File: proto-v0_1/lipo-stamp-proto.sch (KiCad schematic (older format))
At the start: 27 parts, among them Q1 Q_PMOS_GSD, U3 MCP73832-2-OT, U4 AP2112K-3.3, U5 AP9101CK6, U6 FS8205

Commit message: Going to start routing
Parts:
- added D1, D10, D11, D12, D13, D4, D5, D6, D7, D8, D9: LED, LED_SMD:LED_0805_2012Metric, symbol Device:LED
- added JP1, JP2, JP3, JP4: SolderJumper_2_Open, Jumper:SolderJumper-2_P1.3mm_Open_TrianglePad1.0x1.5mm, symbol Jumper:SolderJumper_2_Open
- added JP10, JP11, JP12, JP13, JP14, JP15, JP16, JP5, JP6, JP7, JP8, JP9: Jumper_NC_Small, Jumper:SolderJumper-2_P1.3mm_Bridged_RoundedPad1.0x1.5mm, symbol Device:Jumper_NC_Small
- added R10, R11, R12, R13, R15, R16, R17, R18, R19, R20, R9: R, Resistor_SMD:R_0805_2012Metric, symbol Device:R
- added R14, R6: 10K, Resistor_SMD:R_0805_2012Metric, symbol Device:R
- added R7: 2K2, Resistor_SMD:R_0805_2012Metric, symbol Device:R
- added R8: 1K, Resistor_SMD:R_0805_2012Metric, symbol Device:R
- added TP1, TP11, TP12, TP13, TP2, TP20, TP21, TP22, TP23, TP24, TP25, TP26, TP27, TP28, TP29, TP3, TP30, TP31, TP32, TP33, TP34, TP35, TP36, TP37, TP38, TP4, TP5, TP6: TestPoint, Everything:castellated-2-pin, symbol Connector:TestPoint
- added Z1, Z10, Z11, Z12, Z13, Z14, Z19, Z3, Z4, Z6, Z7, Z9: 0, Resistor_SMD:R_0805_2012Metric, symbol Device:R_Small
- R1: value R -> 4K7
- R3: value 330Ohm -> 330
- TP10, TP14, TP15, TP16, TP17, TP18, TP19, TP7, TP8, TP9: footprint Connector_PinHeader_2.54mm:PinHeader_1x01_P2.54mm_Vertical -> Everything:castellated-2-pin
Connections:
- net +BATT: now also TP16.1, D8.2 (A), TP12.1, TP2.1, TP6.1, Z13.1, Z4.1, Z9.1; no longer C2.1, Q1.3 (D), R3.1, TP15.1, TP8.1, U3.3 (VBAT)
- net +CHARGE: now also TP14.1, D13.2 (A), TP4.1, Z1.2, Z3.2; no longer C1.1, D2.2 (A), D3.2 (A), Q1.1 (G), R5.2, TP10.1, U3.4 (VDD)
- net -BATT: now also JP11.1, TP1.1, TP11.1, Z14.1; no longer C5.2, TP7.1, U5.6 (VSS), U6.1 (S1)
- net 3V3_OUT: now also TP17.1, TP7.1, D11.2 (A), Z12.1; no longer C4.1, TP16.1, U4.5 (VOUT)
- net 3V3_REG_EN: now also TP18.1, TP8.1, D10.2 (A), Z11.2; no longer TP17.1, U4.3 (EN)
- net GND: now also TP10.1, JP10.1, JP13.1, JP14.1, JP15.1, JP16.1, JP5.1, JP7.1, JP8.1, JP9.1, R6.2, R7.2, R8.2, TP13.1, TP20.1, TP3.1, TP30.1, Z19.1; no longer R4.2, TP19.1, TP9.1, U6.3 (S2)
- net STAT_OUT: now also TP19.1, TP9.1, JP12.1, Z6.2; no longer R2.2, TP18.1, U3.1 (STAT)
- net VMAX_OUT: now also TP15.1, D12.2 (A), D9.2 (A), TP5.1, Z10.2, Z7.1; no longer C3.1, D2.1 (K), Q1.2 (S), TP14.1, U4.1 (VIN)
- net at C5.1, R3.2, U5.5 (VDD): now also TP23.1
- net at R4.1, U5.2 (VM): now also TP22.1
- net at U3.5 (PROG): now also JP1.1 (A), JP2.1 (A), JP3.1 (A), JP4.1 (A), TP29.1; no longer R1.1
- net at U5.1 (DO), U6.6 (G1): now also TP25.1
- net at U5.3 (CO), U6.4 (G2): now also TP24.1
- new net: D2.1 (K), Q1.2 (S), TP28.1, Z7.2
- new net: D2.2 (A), Q1.1 (G), R5.2, TP26.1, Z1.1
- new net: Q1.3 (D), TP27.1, Z4.2
- new net: C3.1, D5.2 (A), R14.2, TP36.1, U4.1 (VIN), Z10.1
- new net: C4.1, D6.2 (A), TP38.1, U4.5 (VOUT), Z12.2
- new net: C5.2, TP21.1, U5.6 (VSS), U6.1 (S1), Z14.2
- new net: R4.2, TP34.1, U6.3 (S2), Z19.2
- new net: R3.1, TP35.1, Z13.2
- new net: C2.1, D4.2 (A), TP32.1, U3.3 (VBAT), Z9.2
- new net: C1.1, D1.2 (A), D3.2 (A), TP31.1, U3.4 (VDD), Z3.1
- new net: JP6.2, R2.2
- new net: JP6.1, TP33.1, U3.1 (STAT), Z6.1
- new net: JP2.2 (B), R1.1
- new net: D7.2 (A), R14.1, TP37.1, U4.3 (EN), Z11.1
- new net: JP1.2 (B), R6.1
- new net: JP4.2 (B), R8.1
- new net: JP3.2 (B), R7.1
- new net: D1.1 (K), R9.1
- new net: JP5.2, R9.2
- new net: D4.1 (K), R10.1
- new net: JP7.2, R10.2
- new net: D5.1 (K), R11.1
- new net: JP8.2, R11.2
- new net: D6.1 (K), R12.1
- new net: JP9.2, R12.2
- new net: D7.1 (K), R13.1
- new net: JP10.2, R13.2
- new net: D9.1 (K), R16.1
- new net: JP12.2, R16.2
- new net: D10.1 (K), R17.1
- new net: JP13.2, R17.2
- new net: D11.1 (K), R18.1
- new net: JP14.2, R18.2
- new net: D12.1 (K), R19.1
- new net: JP15.2, R19.2
- new net: D13.1 (K), R20.1
- new net: JP16.2, R20.2
- new net: D8.1 (K), R15.1
- new net: JP11.2, R15.2
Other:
- note added: "1000mA"
- note added: "100mA"
- note added: "213mA"
- note added: "455mA"
- note removed: "TODO: Resistor Values"
- note removed: "TODO: Should -CHARGE be common with GND?"
- note removed: "TODO: Should VBAT be common with +BATT?\nDownstream of battery protection?"
- moved on the sheet: C1, C2, C3, C4, C5, D2, D3, Q1, R1, R2, R3, R4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

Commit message: Almost done, just needs back silkscreen
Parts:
- removed JP11: Jumper_NC_Small, Jumper:SolderJumper-2_P1.3mm_Bridged_RoundedPad1.0x1.5mm, symbol Device:Jumper_NC_Small
- added JP11: Jumper_NO_Small, Jumper:SolderJumper-2_P1.3mm_Open_RoundedPad1.0x1.5mm, symbol Device:Jumper_NO_Small
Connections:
- net -BATT: now also JP11.2
- net at R15.2: now also JP11.1
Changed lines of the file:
@@
 	1    0    0    -1
-$EndComp
-$Comp
-L Device:Jumper_NC_Small JP11
-U 1 1 604FB90A
-P 5000 3500
-F 0 "JP11" V 5046 3453 50  0000 R CNN
-F 1 "Jumper_NC_Small" V 4955 3453 50  0000 R CNN
-F 2 "Jumper:SolderJumper-2_P1.3mm_Bridged_RoundedPad1.0x1.5mm" H 5000 3500 50  0001 C CNN
-F 3 "~" H 5000 3500 50  0001 C CNN
-	1    5000 3500
-	0    -1   -1   0
 $EndComp
 Text Label 5000 2800 1    50   ~ 0
@@
 Text Label 5000 3600 3    50   ~ 0
 -BATT
+$Comp
+L Device:Jumper_NO_Small JP11
+U 1 1 6068AF95
+P 5000 3500
+F 0 "JP11" V 4954 3548 50  0000 L CNN
+F 1 "Jumper_NO_Small" V 5045 3548 50  0000 L CNN
+F 2 "Jumper:SolderJumper-2_P1.3mm_Open_RoundedPad1.0x1.5mm" H 5000 3500 50  0001 C CNN
+F 3 "~" H 5000 3500 50  0001 C CNN
+	1    5000 3500
+	0    1    1    0
+$EndComp
 $EndSCHEMATC

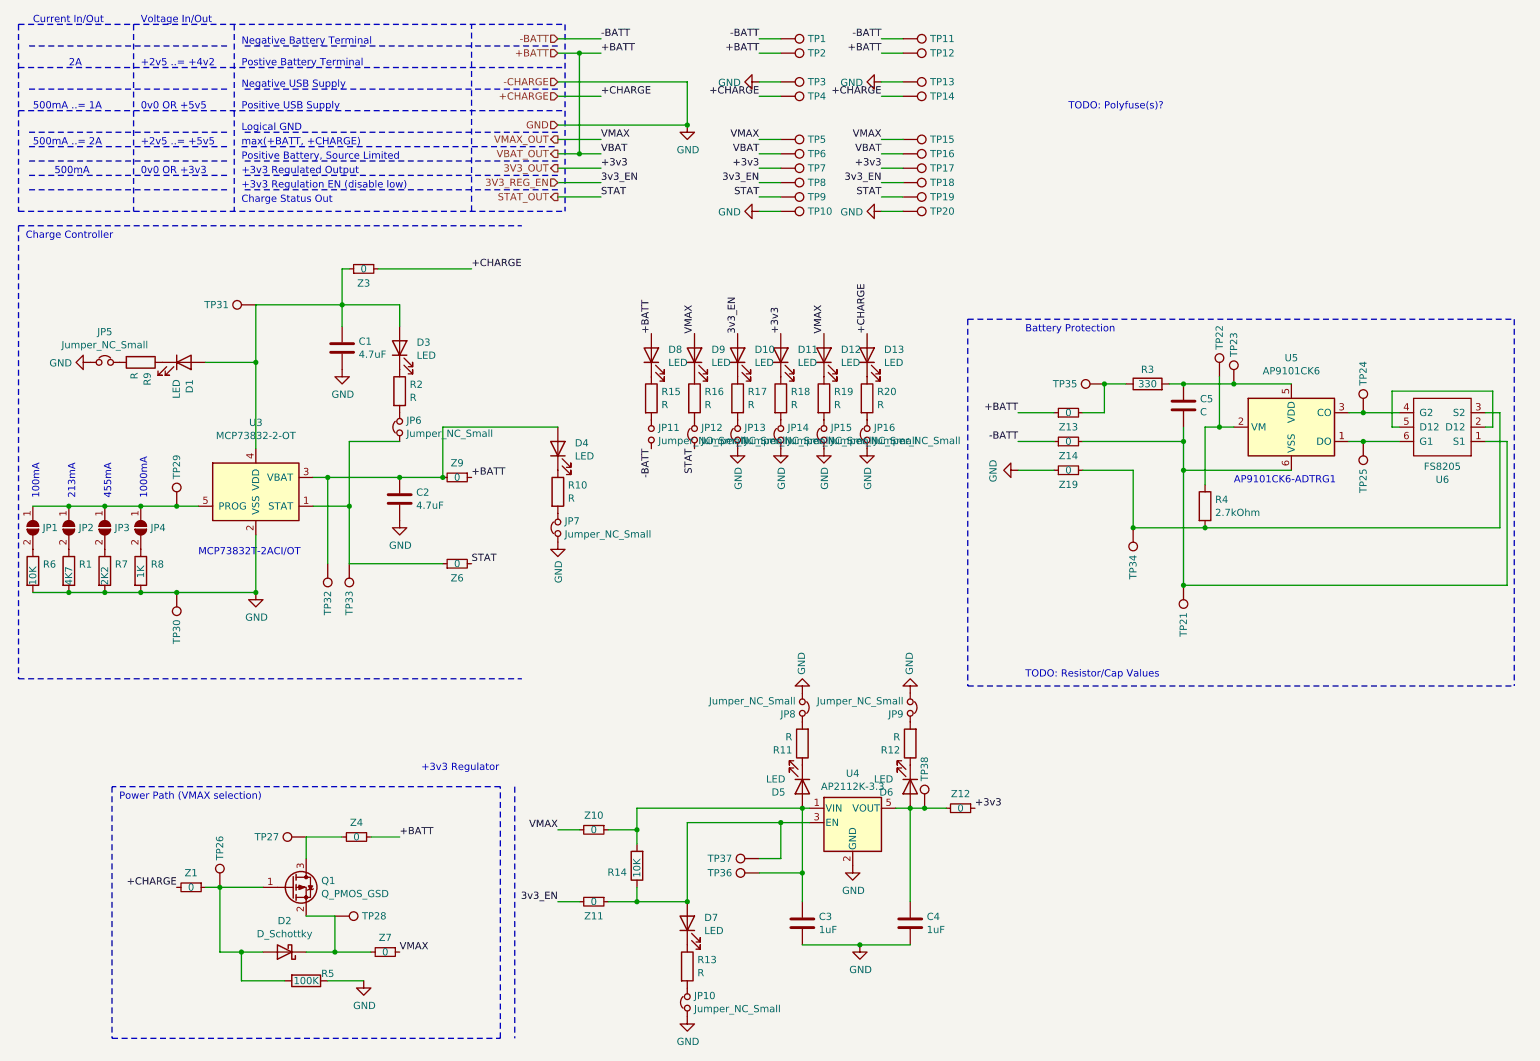
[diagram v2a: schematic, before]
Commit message: Add 2A polyfuse
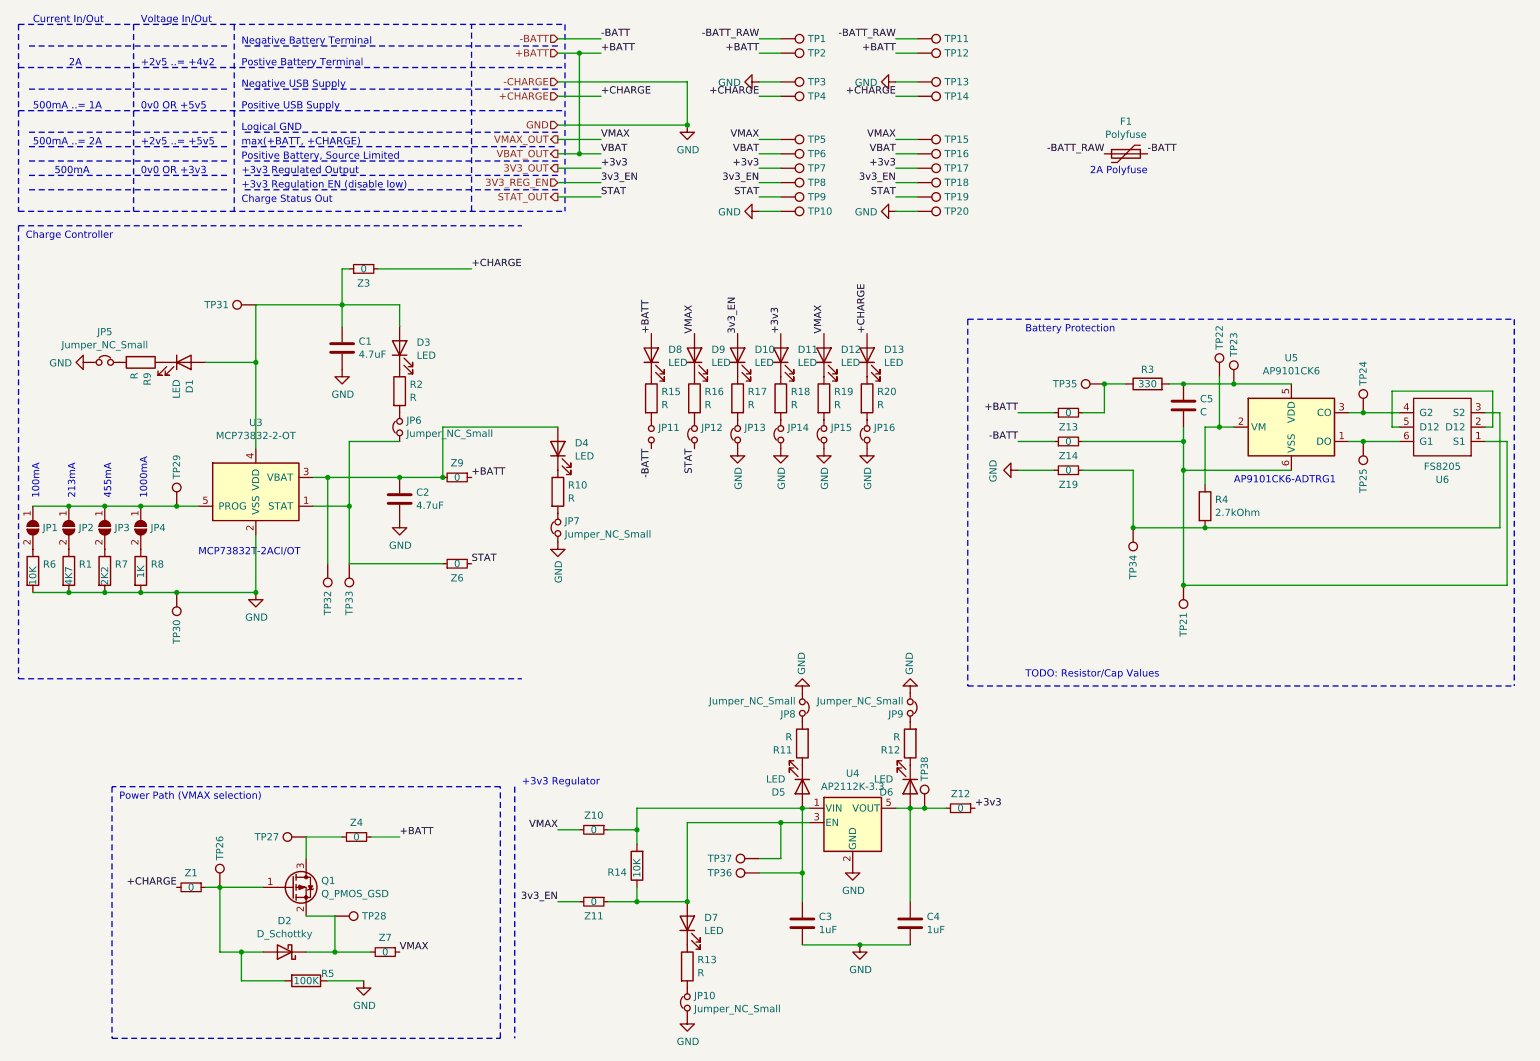
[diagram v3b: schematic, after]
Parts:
- added F1: Polyfuse, Fuse:Fuse_1206_3216Metric_Castellated, symbol Device:Polyfuse
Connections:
- net -BATT: now also F1.1; no longer TP1.1, TP11.1
- new net -BATT_RAW: F1.2, TP1.1, TP11.1
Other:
- note added: "2A Polyfuse"
- note removed: "TODO: Polyfuse(s)?"
- moved on the sheet: TP11, TP12, TP13, TP14, TP15, TP16, TP17, TP18, TP19, TP20

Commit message: Rerouted TP4056, considering redoing
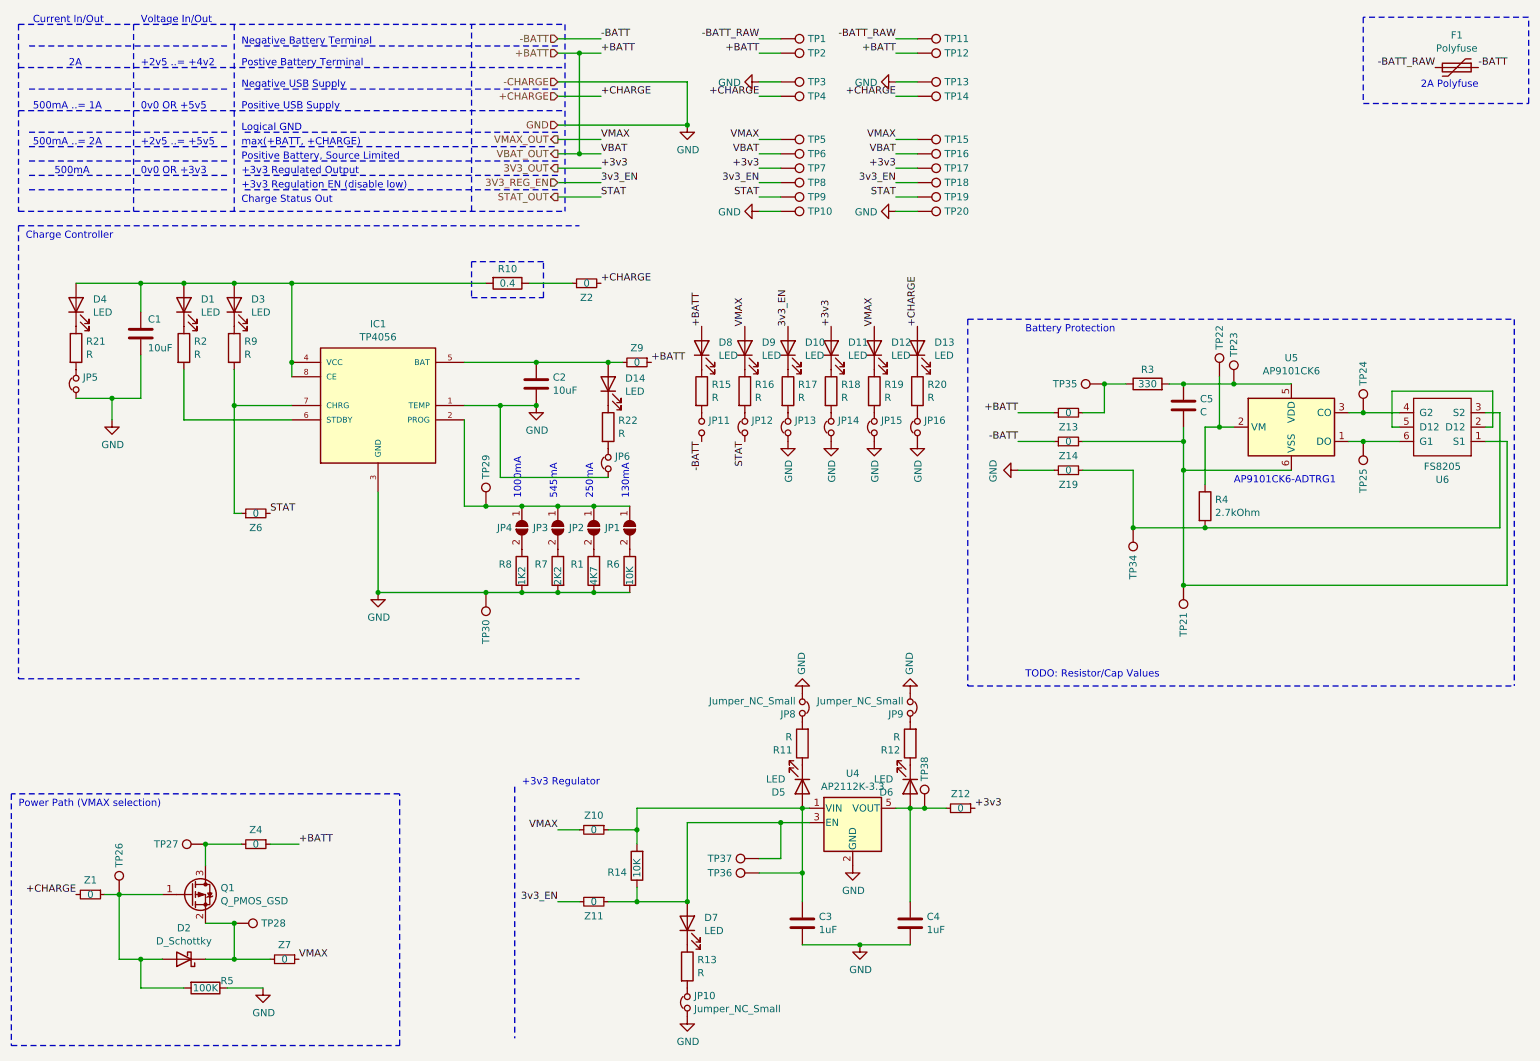
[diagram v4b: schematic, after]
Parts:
- removed JP7: Jumper_NC_Small, Jumper:SolderJumper-2_P1.3mm_Bridged_RoundedPad1.0x1.5mm, symbol Device:Jumper_NC_Small
- removed TP31, TP32, TP33: TestPoint, Everything:castellated-2-pin, symbol Connector:TestPoint
- removed U3: MCP73832-2-OT, Package_TO_SOT_SMD:SOT-23-5, symbol Battery_Management:MCP73832-2-OT
- removed Z3: 0, Resistor_SMD:R_0805_2012Metric, symbol Device:R_Small
- added D14: LED, LED_SMD:LED_0805_2012Metric, symbol Device:LED
- added IC1: TP4056, Everything:SOP-8, symbol Everything:TP4056
- added R21, R22: R, Resistor_SMD:R_0805_2012Metric, symbol Device:R
- added Z2: 0, Resistor_SMD:R_0805_2012Metric, symbol Device:R_Small
- C1, C2: value 4.7uF -> 10uF
- R10: value R -> 0.4
- R8: value 1K -> 1K2
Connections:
- net +CHARGE: now also Z2.2
- net GND: now also JP6.1, IC1.1 (TEMP), IC1.3 (GND)
- net at C2.1, Z9.2: now also D14.2 (A), IC1.5 (BAT); no longer D4.2 (A)
- net at C1.1, D1.2 (A), D3.2 (A): now also D4.2 (A), R10.2, IC1.4 (VCC), IC1.8 (CE)
- net at D3.1 (K): now also R9.1; no longer R2.1
- net at R2.2: now also IC1.6 (STDBY); no longer JP6.2
- net at Z6.1: now also R9.2, IC1.7 (CHRG); no longer JP6.1
- net at JP1.1 (A), JP2.1 (A), JP3.1 (A)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: now also IC1.2 (PROG)
- net at D1.1 (K): now also R2.1; no longer R9.1
- net at JP5.2: now also R21.2; no longer R9.2
- net at R10.1: now also Z2.1; no longer D4.1 (K)
- new net: D4.1 (K), R21.1
- new net: D14.1 (K), R22.1
- new net: JP6.2, R22.2
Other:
- note added: "130mA"
- note added: "250mA"
- note added: "545mA"
- note removed: "100mA"
- note removed: "213mA"
- note removed: "455mA"
- note removed: "MCP73832T-2ACI/OT"
- moved on the sheet: D10, D11, D12, D13, D2, D8, D9, F1, JP1, JP11, JP12, JP13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
